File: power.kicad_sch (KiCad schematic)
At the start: 14 parts, among them U1 B0505S-1WR2, U22 TLV76733DRVx

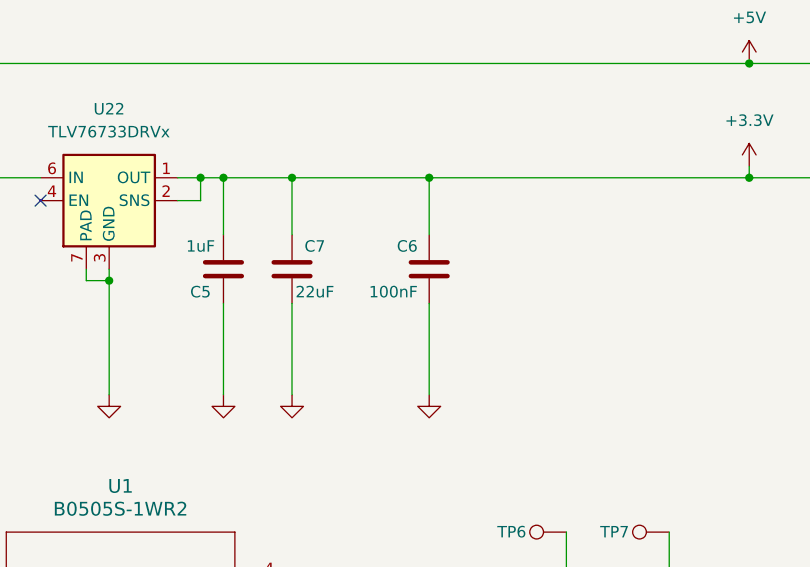
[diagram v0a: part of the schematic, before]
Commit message: smaller caps remove ringing resistors
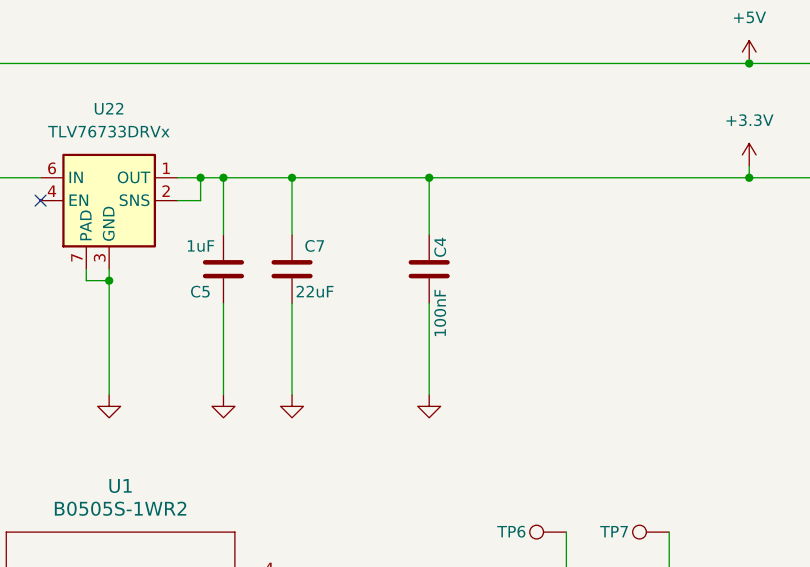
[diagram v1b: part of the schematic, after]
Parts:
- removed C6: 100nF, Capacitor_SMD:C_0603_1608Metric, symbol Device:C
- added C4: 100nF, Capacitor_SMD:C_01005_0402Metric, symbol Device:C
- C7: footprint Capacitor_SMD:C_0603_1608Metric -> Capacitor_SMD:C_0805_2012Metric; LCSC C59461 -> C45783; PageName stm32f407_board -> (none); Voltage (none) -> 25V
- R4: LCSC C21190 -> C22775; Manufacturer StackPole -> (none); Part # RMCF0603JJ1K00 -> (none); VEND DIGI -> (none); VEND# RMCF0603JJ1K00CT-ND -> (none)
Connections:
- net +3.3V: now also C4.1
- net GND: now also C4.2
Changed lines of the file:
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@@
-	)
-	(symbol
-		(lib_id "Device:C")
-		(at 198.12 113.03 0)
-		(mirror y)
-		(unit 1)
-		(exclude_from_sim no)
-		(in_bom yes)
-		(on_board yes)
-		(dnp no)
-		(property "Reference" "C6"
-			(at 196.85 110.49 0)
-			(effects
-				(font
-					(size 1.27 1.27)
-				)
-				(justify left)
-			)
-		)
-		(property "Value" "100nF"
-			(at 196.85 115.57 0)
-			(effects
-				(font
-					(size 1.27 1.27)
-				)
-				(justify left)
-			)
-		)
-		(property "Footprint" "Capacitor_SMD:C_0603_1608Metric"
-			(at 310.388 72.39 90)
-			(effects
-				(font
-					(size 1.524 1.524)
-				)
-				(hide yes)
-			)
-		)
-		(property "Datasheet" "~"
-			(at 198.12 113.03 0)
-			(effects
-				(font
-					(size 1.524 1.524)
-				)
-				(hide yes)
-			)
-		)
-		(property "Description" "Unpolarized capacitor"
-			(at 198.12 113.03 0)
-			(effects
-				(font
-					(size 1.27 1.27)
-				)
-				(hide yes)
-			)
-		)
-		(property "PageName" "stm32f407_board"
-			(at 17.78 83.185 0)
-			(effects
-				(font
-					(size 1.524 1.524)
-				)
-				(hide yes)
-			)
-		)
-		(property "Part #" "C0603C104J5RACTU"
-			(at 584.2 203.2 0)
-			(effects
-				(font
-					(size 1.27 1.27)
-				)
-				(hide yes)
-			)
-		)
-		(property "VEND" "DIGI"
-			(at 584.2 203.2 0)
-			(effects
-				(font
-					(size 1.27 1.27)
-				)
-				(hide yes)
-			)
-		)
-		(property "VEND#" "399-7844-1-ND"
-			(at 584.2 203.2 0)
-			(effects
-				(font
-					(size 1.27 1.27)
-				)
-				(hide yes)
-			)
-		)
-		(property "Manufacturer" "KEMET"
-			(at 584.2 203.2 0)
-			(effects
-				(font
-					(size 1.27 1.27)
-				)
-				(hide yes)
-			)
-		)
-		(property "LCSC" "C14663"
-			(at 198.12 113.03 0)
-			(effects
-				(font
-					(size 1.27 1.27)
-				)
-				(hide yes)
-			)
-		)
-		(property "Sim.Device" ""
-			(at 198.12 113.03 0)
-			(effects
-				(font
-					(size 1.27 1.27)
-				)
-				(hide yes)
-			)
-		)
-		(property "Sim.Pins" ""
-			(at 198.12 113.03 0)
-			(effects
-				(font
-					(size 1.27 1.27)
-				)
-				(hide yes)
-			)
-		)
-		(pin "1"
-		)
-		(pin "2"
-		)
-		(instances
-			(project "l8-kicad"
-				(path "/8d063f79-9282-4820-bcf4-1ff3c006cf08/cb7fc79f-a21e-4f3e-a003-80932d60a7a0"
-					(reference "C6")
-					(unit 1)
-				)
-			)
-		)
 	)
 	(symbol
@@
 			)
 		)
-		(property "LCSC" "C21190"
+		(property "LCSC" "C22775"
 			(at 101.6 90.17 0)
 			(effects
@@
 			)
 		)
-		(property "Manufacturer" "StackPole"
+		(property "Manufacturer" ""
 			(at 101.6 90.17 0)
 			(effects
@@
 			)
 		)
-		(property "Part #" "RMCF0603JJ1K00"
+		(property "Part #" ""
 			(at 101.6 90.17 0)
 			(effects
@@
 			)
 		)
-		(property "VEND" "DIGI"
+		(property "VEND" ""
 			(at 101.6 90.17 0)
 			(effects
@@
 			)
 		)
-		(property "VEND#" "RMCF0603JJ1K00CT-ND"
+		(property "VEND#" ""
 			(at 101.6 90.17 0)
 			(effects
@@
 	)
 	(symbol
+		(lib_id "Device:C")
+		(at 198.12 113.03 0)
+		(unit 1)
+		(exclude_from_sim no)
+		(in_bom yes)
+		(on_board yes)
+		(dnp no)
+		(property "Reference" "C4"
+			(at 199.39 111.76 90)
+			(effects
+				(font
+					(size 1.27 1.27)
+				)
+				(justify left)
+			)
+		)
+		(property "Value" "100nF"
+			(at 199.39 120.65 90)
+			(effects
+				(font
+					(size 1.27 1.27)
+				)
+				(justify left)
+			)
+		)
+		(property "Footprint" "Capacitor_SMD:C_01005_0402Metric"
+			(at 78.232 72.39 90)
+			(effects
+				(font
+					(size 1.524 1.524)
+				)
+				(hide yes)
+			)
+		)
+		(property "Datasheet" "~"
+			(at 198.12 113.03 0)
+			(effects
+				(font
+					(size 1.524 1.524)
+				)
+				(hide yes)
+			)
+		)
+		(property "Description" "Unpolarized capacitor X7R"
+			(at 198.12 113.03 0)
+			(effects
+				(font
+					(size 1.27 1.27)
+				)
+				(hide yes)
+			)
+		)
+		(property "LCSC" "C1525"
+			(at 198.12 113.03 0)
+			(effects
+				(font
+					(size 1.27 1.27)
+				)
+				(hide yes)
+			)
+		)
+		(property "Manufacturer" "Samsung"
+			(at 198.12 113.03 0)
+			(effects
+				(font
+					(size 1.27 1.27)
+				)
+				(hide yes)
+			)
+		)
+		(property "Sim.Device" ""
+			(at 198.12 113.03 0)
+			(effects
+				(font
+					(size 1.27 1.27)
+				)
+				(hide yes)
+			)
+		)
+		(property "Sim.Pins" ""
+			(at 198.12 113.03 0)
+			(effects
+				(font
+					(size 1.27 1.27)
+				)
+				(hide yes)
+			)
+		)
+		(property "Voltage" "16V"
+			(at 198.12 113.03 90)
+			(effects
+				(font
+					(size 1.27 1.27)
+				)
+				(hide yes)
+			)
+		)
+		(pin "1"
+		)
+		(pin "2"
+		)
+		(instances
+			(project "l8-kicad"
+				(path "/8d063f79-9282-4820-bcf4-1ff3c006cf08/cb7fc79f-a21e-4f3e-a003-80932d60a7a0"
+					(reference "C4")
+					(unit 1)
+				)
+			)
+		)
+	)
+	(symbol
 		(lib_id "l8-kicad-rescue:GND-power")
 		(at 78.74 109.22 0)
@@
 			)
 		)
-		(property "Footprint" "Capacitor_SMD:C_0603_1608Metric"
+		(property "Footprint" "Capacitor_SMD:C_0805_2012Metric"
 			(at 96.012 80.01 90)
 			(effects
@@
 			)
 		)
-		(property "PageName" "stm32f407_board"
-			(at 388.62 90.805 0)
-			(effects
-				(font
-					(size 1.524 1.524)
-				)
-				(hide yes)
-			)
-		)
-		(property "LCSC" "C59461"
+		(property "LCSC" " C45783"
 			(at 182.88 113.03 0)
 			(effects
@@
 			(at 182.88 113.03 0)
 			(effects
+				(font
+					(size 1.27 1.27)
+				)
+				(hide yes)
+			)
+		)
+		(property "Voltage" "25V"
+			(at 182.88 113.03 0)
+			(effects

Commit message: usb sheet
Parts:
- PS1: now not fitted
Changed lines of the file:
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@@
 		(in_bom yes)
 		(on_board yes)
-		(dnp no)
+		(dnp yes)
 		(fields_autoplaced yes)
 		(property "Reference" "PS1"

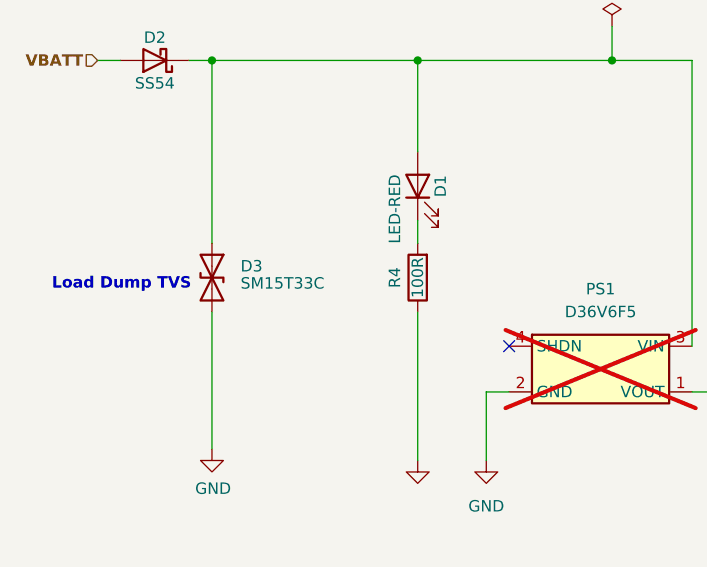
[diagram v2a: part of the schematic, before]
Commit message: smaller test pads
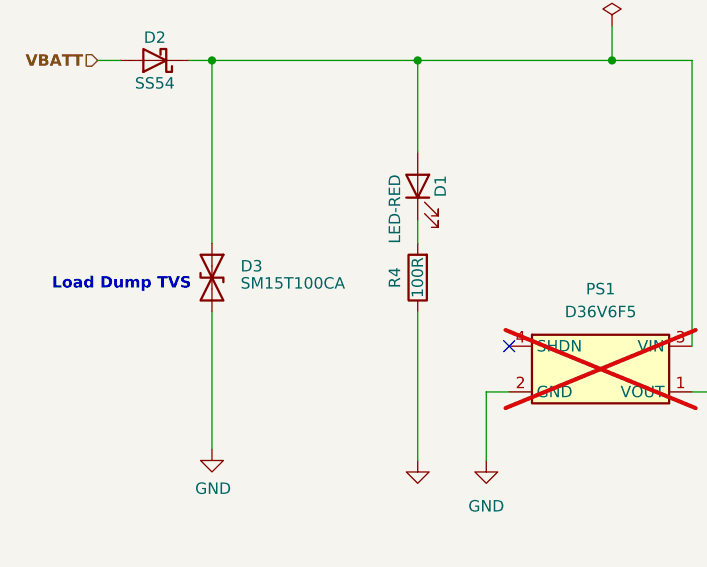
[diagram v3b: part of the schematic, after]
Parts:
- D3: value SM15T33C -> SM15T100CA; LCSC C133707 -> C1975873
- TP1, TP2, TP6, TP7: footprint TestPoint:TestPoint_Pad_D1.0mm -> dnt:TestPoint_Pad_D1.0mm FP .6R
- U22: LCSC (none) -> C2848334
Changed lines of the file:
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@@
 			)
 		)
-		(property "Footprint" "TestPoint:TestPoint_Pad_D1.0mm"
+		(property "Footprint" "dnt:TestPoint_Pad_D1.0mm FP .6R"
 			(at 213.36 137.16 0)
 			(effects
@@
 		)
 		(property "Sim.Pins" ""
+			(at 213.36 142.24 0)
+			(effects
+				(font
+					(size 1.27 1.27)
+				)
+				(hide yes)
+			)
+		)
+		(property "Silkscreen" ""
 			(at 213.36 142.24 0)
 			(effects
@@
 			)
 		)
+		(property "Silkscreen" ""
+			(at 72.39 66.04 0)
+			(effects
+				(font
+					(size 1.27 1.27)
+				)
+				(hide yes)
+			)
+		)
 		(pin "1"
 		)
@@
 			)
 		)
-		(property "Footprint" "TestPoint:TestPoint_Pad_D1.0mm"
+		(property "Footprint" "dnt:TestPoint_Pad_D1.0mm FP .6R"
 			(at 224.79 137.16 0)
 			(effects
@@
 		)
 		(property "Sim.Pins" ""
+			(at 224.79 142.24 0)
+			(effects
+				(font
+					(size 1.27 1.27)
+				)
+				(hide yes)
+			)
+		)
+		(property "Silkscreen" ""
 			(at 224.79 142.24 0)
 			(effects
@@
 			)
 		)
+		(property "Silkscreen" ""
+			(at 101.6 90.17 0)
+			(effects
+				(font
+					(size 1.27 1.27)
+				)
+				(hide yes)
+			)
+		)
 		(pin "1"
 		)
@@
 			)
 		)
+		(property "Silkscreen" ""
+			(at 198.12 113.03 0)
+			(effects
+				(font
+					(size 1.27 1.27)
+				)
+				(hide yes)
+			)
+		)
 		(pin "1"
 		)
@@
 			)
 		)
-		(property "Value" "SM15T33C"
+		(property "Value" "SM15T100CA"
 			(at 81.915 90.805 90)
 			(effects
@@
 			)
 		)
-		(property "LCSC" "C133707"
+		(property "LCSC" "C1975873"
 			(at 78.74 90.17 0)
 			(effects
@@
 		)
 		(property "Sim.Pins" ""
+			(at 78.74 90.17 0)
+			(effects
+				(font
+					(size 1.27 1.27)
+				)
+				(hide yes)
+			)
+		)
+		(property "Silkscreen" ""
 			(at 78.74 90.17 0)
 			(effects
@@
 			)
 		)
-		(property "Footprint" "TestPoint:TestPoint_Pad_D1.0mm"
+		(property "Footprint" "dnt:TestPoint_Pad_D1.0mm FP .6R"
 			(at 251.46 95.25 0)
 			(effects
@@
 		)
 		(property "Sim.Pins" ""
+			(at 251.46 90.17 0)
+			(effects
+				(font
+					(size 1.27 1.27)
+				)
+				(hide yes)
+			)
+		)
+		(property "Silkscreen" ""
 			(at 251.46 90.17 0)
 			(effects
@@
 			)
 		)
+		(property "Silkscreen" ""
+			(at 101.6 80.01 0)
+			(effects
+				(font
+					(size 1.27 1.27)
+				)
+				(hide yes)
+			)
+		)
 		(pin "1"
 		)
@@
 			)
 		)
-		(property "Footprint" "TestPoint:TestPoint_Pad_D1.0mm"
+		(property "Footprint" "dnt:TestPoint_Pad_D1.0mm FP .6R"
 			(at 251.46 107.95 0)
 			(effects
@@
 		)
 		(property "Sim.Pins" ""
+			(at 251.46 102.87 0)
+			(effects
+				(font
+					(size 1.27 1.27)
+				)
+				(hide yes)
+			)
+		)
+		(property "Silkscreen" ""
 			(at 251.46 102.87 0)
 			(effects
@@
 			)
 		)
+		(property "Silkscreen" ""
+			(at 121.92 100.33 0)
+			(effects
+				(font
+					(size 1.27 1.27)
+				)
+				(hide yes)
+			)
+		)
 		(pin "3"
 		)
@@
 			)
 		)
+		(property "Silkscreen" ""
+			(at 175.26 113.03 0)
+			(effects
+				(font
+					(size 1.27 1.27)
+				)
+				(hide yes)
+			)
+		)
 		(pin "1"
 		)
@@
 		)
 		(property "Voltage" "25V"
+			(at 182.88 113.03 0)
+			(effects
+				(font
+					(size 1.27 1.27)
+				)
+				(hide yes)
+			)
+		)
+		(property "Silkscreen" ""
 			(at 182.88 113.03 0)
 			(effects
@@
 			)
 		)
+		(property "Silkscreen" ""
+			(at 143.51 147.32 0)
+			(effects
+				(font
+					(size 1.27 1.27)
+				)
+				(hide yes)
+			)
+		)
 		(pin "2"
 		)
@@
 			(at 162.56 105.41 0)
 			(effects
+				(font
+					(size 1.27 1.27)
+				)
+				(hide yes)
+			)
+		)
+		(property "LCSC" "C2848334"
+			(at 162.56 105.41 0)
+			(effects
+				(font
+					(size 1.27 1.27)
+				)
+				(hide yes)
+			)
+		)
+		(property "Silkscreen" ""
+			(at 162.56 105.41 0)
+			(effects

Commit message: pre-quilter after cap size issue
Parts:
- C4: footprint Capacitor_SMD:C_01005_0402Metric -> Capacitor_SMD:C_0603_1608Metric; LCSC C1525 -> (none); Manufacturer Samsung -> (none); Voltage 16V -> (none)
- D2: footprint Diode_SMD:D_SMC -> Diode_SMD:D_SMA; Silkscreen (none) -> X
- TP1, TP2, TP6, TP7: now left out of the parts list
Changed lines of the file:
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@@
 		(unit 1)
 		(exclude_from_sim no)
-		(in_bom yes)
+		(in_bom no)
 		(on_board yes)
 		(dnp no)
@@
 			)
 		)
-		(property "Footprint" "Diode_SMD:D_SMC"
+		(property "Footprint" "Diode_SMD:D_SMA"
 			(at 72.39 61.595 0)
 			(effects
@@
 			)
 		)
-		(property "Datasheet" "http://www.jameco.com/Jameco/Products/ProdDS/1538777.pdf"
+		(property "Datasheet" "https://wmsc.lcsc.com/wmsc/upload/file/pdf/v2/lcsc/2303141100_MDD-Microdiode-Electronics-SS54_C22452.pdf"
 			(at 72.39 66.04 0)
 			(effects
@@
 			)
 		)
-		(property "Description" "40V 3A Schottky Barrier Rectifier Diode, SMC"
+		(property "Description" " 40V 550mV@5A 5A SMA(DO-214AC) Schottky Barrier Diodes (SBD) ROHS"
 			(at 72.39 66.04 0)
 			(effects
@@
 			)
 		)
-		(property "Silkscreen" ""
+		(property "Silkscreen" "X"
 			(at 72.39 66.04 0)
 			(effects
@@
 		(unit 1)
 		(exclude_from_sim no)
-		(in_bom yes)
+		(in_bom no)
 		(on_board yes)
 		(dnp no)
@@
 			)
 		)
-		(property "Footprint" "Capacitor_SMD:C_01005_0402Metric"
+		(property "Footprint" "Capacitor_SMD:C_0603_1608Metric"
 			(at 78.232 72.39 90)
 			(effects
@@
 			)
 		)
-		(property "LCSC" "C1525"
+		(property "LCSC" ""
 			(at 198.12 113.03 0)
 			(effects
@@
 			)
 		)
-		(property "Manufacturer" "Samsung"
+		(property "Manufacturer" ""
 			(at 198.12 113.03 0)
 			(effects
@@
 			)
 		)
-		(property "Voltage" "16V"
+		(property "Voltage" ""
 			(at 198.12 113.03 90)
 			(effects
@@
 		(unit 1)
 		(exclude_from_sim no)
-		(in_bom yes)
+		(in_bom no)
 		(on_board yes)
 		(dnp no)
@@
 		(unit 1)
 		(exclude_from_sim no)
-		(in_bom yes)
-		(on_board yes)
-		(dnp no)
+		(in_bom no)
+		(on_board yes)
+		(dnp no)

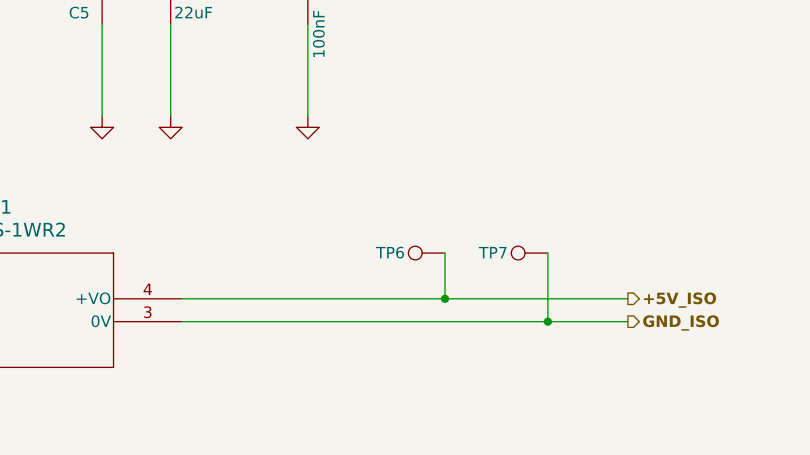
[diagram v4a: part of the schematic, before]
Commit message: remove tp and rotate cpu
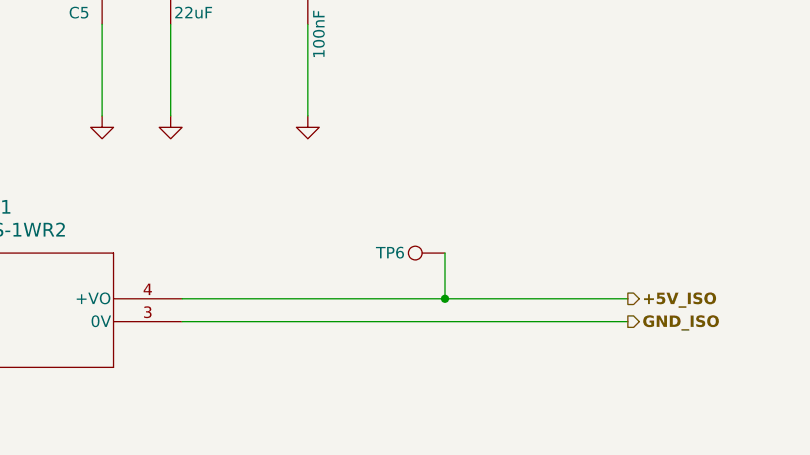
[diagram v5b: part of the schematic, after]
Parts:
- removed TP7: GND ISO, dnt:TestPoint_Pad_D1.0mm FP .6R, symbol Connector:TestPoint
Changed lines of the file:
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@@
-	)
-	(junction
-		(at 224.79 149.86)
-		(diameter 0)
-		(color 0 0 0 0)
 	)
 	(junction
@@
 	(wire
 		(pts
-			(xy 184.15 149.86) (xy 224.79 149.86)
+			(xy 184.15 149.86) (xy 233.68 149.86)
 		)
 		(stroke
@@
 	(wire
 		(pts
-			(xy 224.79 142.24) (xy 224.79 149.86)
-		)
-		(stroke
-			(width 0)
-			(type default)
-		)
-	)
-	(wire
-		(pts
 			(xy 198.12 102.87) (xy 233.68 102.87)
 		)
@@
 		(pts
 			(xy 130.81 147.32) (xy 143.51 147.32)
-		)
-		(stroke
-			(width 0)
-			(type default)
-		)
-	)
-	(wire
-		(pts
-			(xy 224.79 149.86) (xy 233.68 149.86)
 		)
 		(stroke
@@
 					(unit 1)
 				)
-			)
-		)
-	)
-	(symbol
-		(lib_id "Connector:TestPoint")
-		(at 224.79 142.24 90)
-		(unit 1)
-		(exclude_from_sim no)
-		(in_bom no)
-		(on_board yes)
-		(dnp no)
-		(property "Reference" "TP7"
-			(at 220.345 142.24 90)
-			(effects
-				(font
-					(size 1.27 1.27)
-				)
-				(justify left)
-			)
-		)
-		(property "Value" "GND ISO"
-			(at 215.265 142.24 90)
-			(effects
-				(font
-					(size 1.27 1.27)
-				)
-				(justify left)
-				(hide yes)
-			)
-		)
-		(property "Footprint" "dnt:TestPoint_Pad_D1.0mm FP .6R"
-			(at 224.79 137.16 0)
-			(effects
-				(font
-					(size 1.27 1.27)
-				)
-				(hide yes)
-			)
-		)
-		(property "Datasheet" "~"
-			(at 224.79 137.16 0)
-			(effects
-				(font
-					(size 1.27 1.27)
-				)
-				(hide yes)
-			)
-		)
-		(property "Description" "GND ISO"
-			(at 224.79 142.24 0)
-			(effects
-				(font
-					(size 1.27 1.27)
-				)
-				(hide yes)
-			)
-		)
-		(property "Part #" "DNP"
-			(at 370.205 356.87 0)
-			(effects
-				(font
-					(size 1.27 1.27)
-				)
-				(hide yes)
-			)
-		)
-		(property "VEND" "DNP"
-			(at 370.205 356.87 0)
-			(effects
-				(font
-					(size 1.27 1.27)
-				)
-				(hide yes)
-			)
-		)
-		(property "VEND#" "DNP"
-			(at 370.205 356.87 0)
-			(effects
-				(font
-					(size 1.27 1.27)
-				)
-				(hide yes)
-			)
-		)
-		(property "Manufacturer" "DNP"
-			(at 370.205 356.87 0)
-			(effects
-				(font
-					(size 1.27 1.27)
-				)
-				(hide yes)
-			)
-		)
-		(property "Sim.Device" ""
-			(at 224.79 142.24 0)
-			(effects
-				(font
-					(size 1.27 1.27)
-				)
-				(hide yes)
-			)
-		)
-		(property "Sim.Pins" ""
-			(at 224.79 142.24 0)
-			(effects
-				(font
-					(size 1.27 1.27)
-				)
-				(hide yes)
-			)
-		)
-		(property "Silkscreen" ""
-			(at 224.79 142.24 0)
-			(effects
-				(font
-					(size 1.27 1.27)
-				)
-				(hide yes)
-			)
-		)
-		(pin "1"
-		)
-		(instances
-			(project "l8-kicad"
-				(path "/8d063f79-9282-4820-bcf4-1ff3c006cf08/cb7fc79f-a21e-4f3e-a003-80932d60a7a0"
-					(reference "TP7")
-					(unit 1)
-				)

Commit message: pre JLCPCB try 1
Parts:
- C4: LCSC (none) -> C14663
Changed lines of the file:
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@@
 			)
 		)
-		(property "LCSC" ""
+		(property "LCSC" "C14663"
 			(at 198.12 113.03 0)
 			(effects

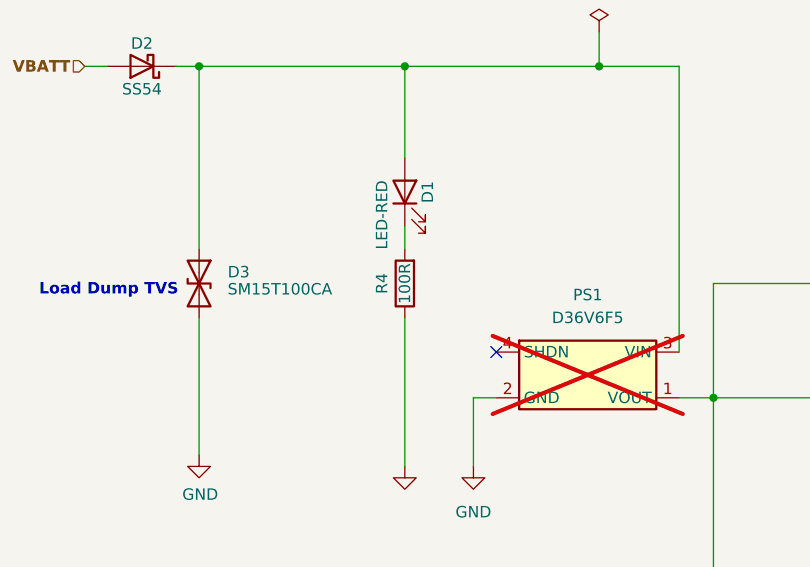
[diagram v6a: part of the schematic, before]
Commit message: change to 2.2k for 12v LED
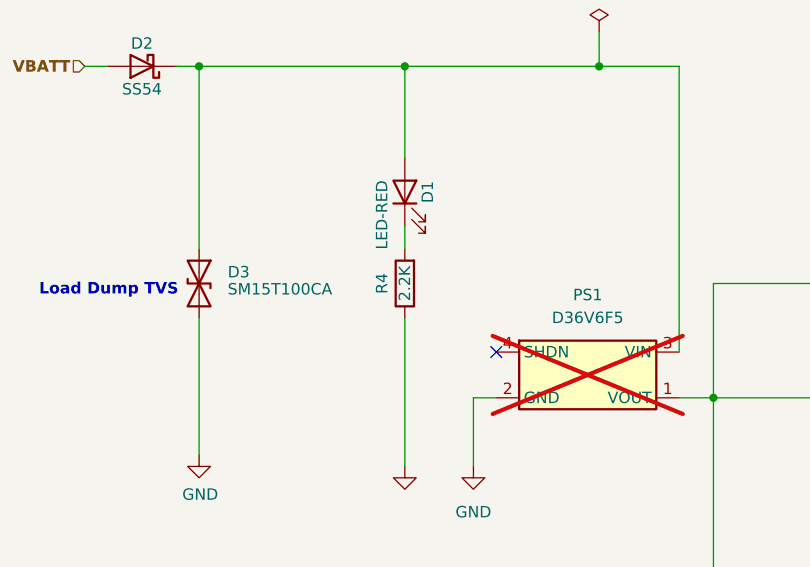
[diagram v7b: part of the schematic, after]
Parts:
- R4: value 100R -> 2.2K; LCSC C22775 -> C4190
- U1: LCSC (none) -> C C2992393
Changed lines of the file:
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@@
 			)
 		)
-		(property "Value" "100R"
+		(property "Value" "2.2K"
 			(at 101.6 90.17 90)
 			(effects
@@
 			)
 		)
-		(property "LCSC" "C22775"
+		(property "LCSC" "C4190"
 			(at 101.6 90.17 0)
 			(effects
@@
 			(at 143.51 147.32 0)
 			(effects
+				(font
+					(size 1.27 1.27)
+				)
+				(hide yes)
+			)
+		)
+		(property "LCSC" "C C2992393"
+			(at 143.51 147.32 0)
+			(effects

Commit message: SENT TO jlcpcb
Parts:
- D1, D2: JLCPCB Rotation Offset (none) -> 180
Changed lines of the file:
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@@
+			)
+		)
+		(property "JLCPCB Rotation Offset" "180"
+			(at 72.39 66.04 0)
+			(effects
+				(font
+					(size 1.27 1.27)
+				)
+				(hide yes)
 			)
 		)
@@
 			(at 101.6 80.01 0)
 			(effects
+				(font
+					(size 1.27 1.27)
+				)
+				(hide yes)
+			)
+		)
+		(property "JLCPCB Rotation Offset" "180"
+			(at 101.6 80.01 0)
+			(effects
